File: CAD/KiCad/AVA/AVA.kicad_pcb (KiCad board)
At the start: 2 copper layers, 100 x 75 mm, 47 parts, among them J1 Conn_01x03_Pin, J10 Conn_01x04_Pin, J2 Conn_01x03_Pin, J3 Conn_01x03_Pin, J4 Conn_01x03_Pin, J5 Conn_01x02_Pin, J6 Conn_01x02_Pin, J7 Conn_01x02_Pin, J8 Conn_01x03_Pin, J9 Conn_01x03_Pin

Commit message: Using correct footprint now. Jarvis, more alcohol
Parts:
- added U1: ~, AVA:ESP32-C3-Super-Mini, F.Cu at (204.3, 72.9)
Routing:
- net Net-(U1-D2): track 22.7 -> 114.5 mm
- net Net-(U1-D3): track 30.8 -> 113.2 mm
- net Net-(U1-D1): track 42.5 -> 123.6 mm
- net Net-(U1-D0): track 50.0 -> 127.5 mm
- net Net-(U1-3.3V): track 86.0 -> 138.7 mm
- net Net-(U1-RX): track 0.00 -> 51.6 mm
- net Net-(U1-TX): track 0.00 -> 49.1 mm
- net Net-(J1-Pin_1): track 171.4 -> 214.3 mm
- net (no net): track 41.1 -> 0.00 mm, vias 6 -> 0
- net GND: track 0.00 -> 40.4 mm, vias 0 -> 6
- net Net-(A1-D1/TX): track 52.9 -> 79.5 mm
- net Net-(A1-D0/RX): track 46.7 -> 65.7 mm
- net Net-(U1-D10): track 52.8 -> 37.4 mm
- added copper zone on B.Cu, net GND
- removed copper zone on B.Cu, net (none)

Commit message: Back, front finished. Cropped svg for printing, 500 cigarettes
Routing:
- net GND: vias 6 -> 8
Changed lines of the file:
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@@
 			(dxfimperialunits yes)
 			(dxfusepcbnewfont yes)
-			(psnegative no)
+			(psnegative yes)
 			(psa4output no)
 			(plot_black_and_white yes)
@@
 			(crossoutdnponfab yes)
 			(subtractmaskfromsilk no)
-			(outputformat 2)
+			(outputformat 5)
 			(mirror no)
 			(drillshape 0)
 			(scaleselection 1)
-			(outputdirectory "FAB/DRL/")
+			(outputdirectory "FAB/SVG/")
 		)
 	)
@@
 	)
 	(segment
+		(start 163.83 94.615)
+		(end 163.83 104.565)
+		(width 0.8)
+		(layer "F.Cu")
+		(net "GND")
+	)
+	(segment
 		(start 163.83 70.485)
 		(end 163.83 62.23)
@@
 	(segment
 		(start 163.83 84.455)
-		(end 163.83 104.565)
+		(end 163.83 92.71)
 		(width 0.8)
 		(layer "F.Cu")
@@
 		(net "GND")
 	)
+	(segment
+		(start 163.83 92.71)
+		(end 163.83 94.615)
+		(width 0.8)
+		(layer "F.Cu")
+		(net "GND")
+	)
 	(via
 		(at 163.83 104.565)
@@
 	)
 	(via
+		(at 163.83 92.71)
+		(size 1.6)
+		(drill 0.8)
+		(layers "F.Cu" "B.Cu")
+		(net "GND")
+	)
+	(via
 		(at 163.83 70.485)
 		(size 1.6)
@@
 		(net "GND")
 	)
+	(via
+		(at 163.83 94.615)
+		(size 1.6)
+		(drill 0.8)
+		(layers "F.Cu" "B.Cu")
+		(net "GND")
+	)

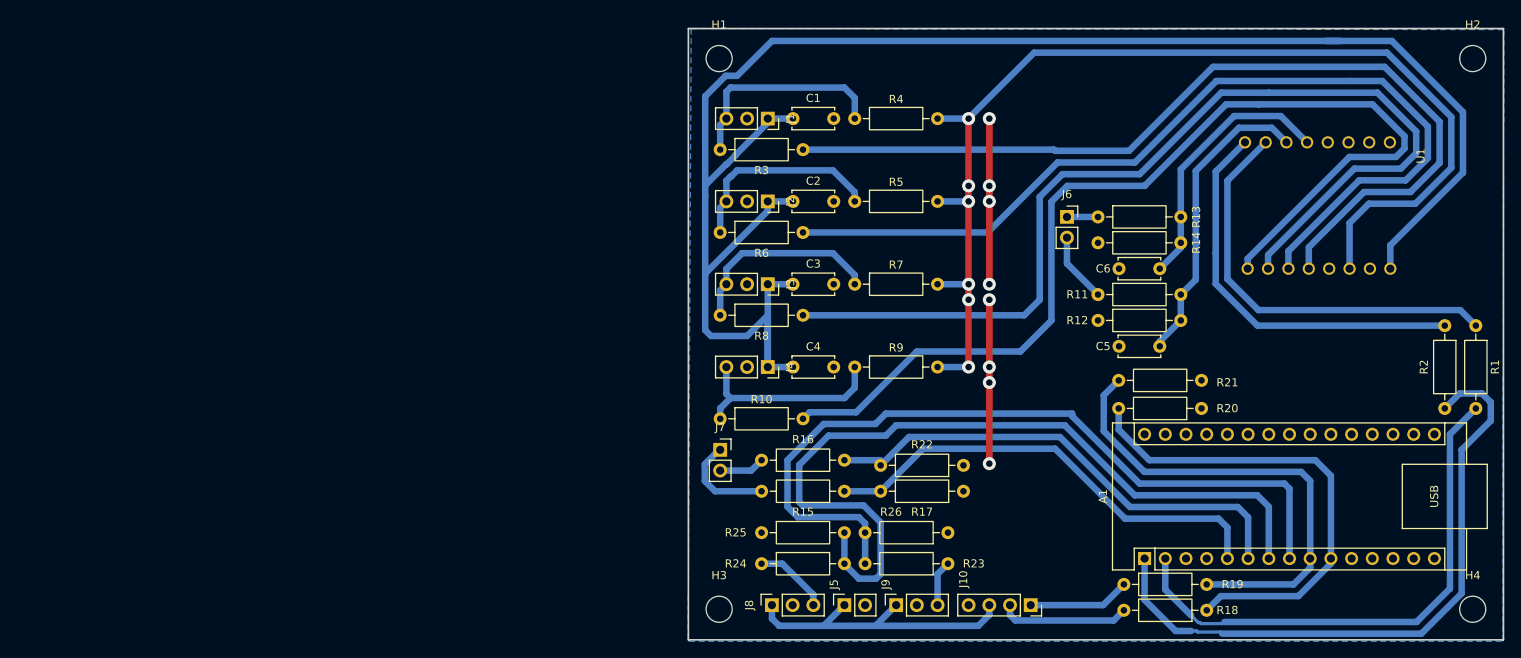
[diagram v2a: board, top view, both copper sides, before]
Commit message: Track width min now 1.6mm. Double sided board, no pre-drawn holes in front, back svg for easy printing
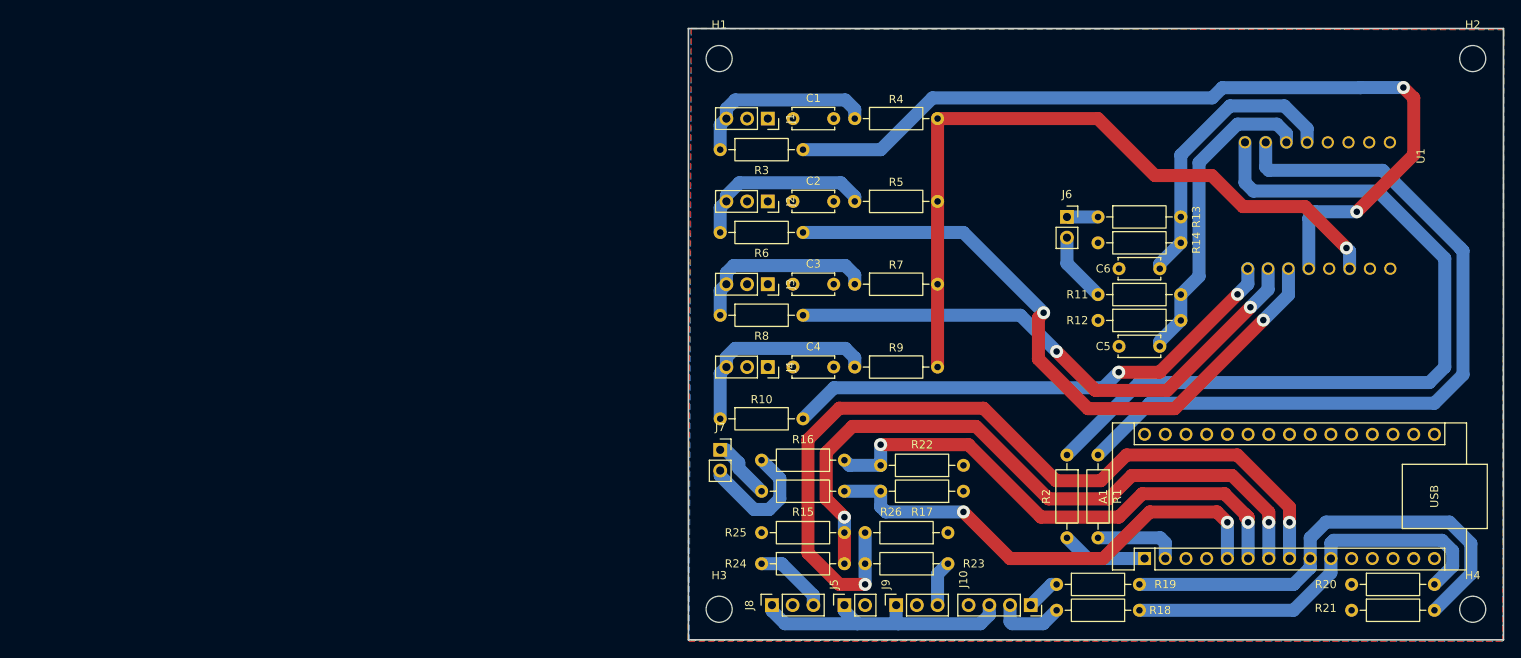
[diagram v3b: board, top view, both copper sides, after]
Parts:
- moved R1 49.0 mm to (177.2, 103.5)
- moved R2 49.0 mm to (173.4, 103.5)
- moved R21 33.7 mm to (208.3, 122.6), turned to 0 degrees
- moved R20 28.4 mm to (208.3, 119.4), turned to 0 degrees
- moved R18 8.25 mm to (182.2, 122.6)
- moved R19 8.25 mm to (172.1, 119.4)
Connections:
- net Net-(J1-Pin_1) renamed VCC
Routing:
- net VCC: track 214.3 -> 0.00 mm
- net Net-(A1-D1/TX): track 79.5 -> 10.6 mm
- net Net-(U1-D0): track 127.5 -> 63.3 mm, vias 0 -> 2
- net Net-(A1-D0/RX): track 65.7 -> 10.4 mm
- net Net-(U1-D1): track 123.6 -> 68.6 mm, vias 0 -> 2
- net Net-(U1-3.3V): track 138.7 -> 89.9 mm, vias 6 -> 1
- net Net-(U1-TX): track 49.1 -> 97.5 mm
- net Net-(U1-RX): track 51.6 -> 95.6 mm
- net GND: track 40.4 -> 0.00 mm, vias 8 -> 0
- net Net-(U1-D2): track 114.5 -> 81.7 mm, vias 0 -> 2
- net Net-(A1-D4): track 101.3 -> 82.6 mm, vias 0 -> 2
- net Net-(J7-Pin_2): track 5.61 -> 15.9 mm
- net Net-(A1-D7): track 59.4 -> 49.7 mm
- net /CH1: track 12.5 -> 4.23 mm
- net /CH2: track 16.0 -> 8.53 mm
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- added copper zone on F.Cu, net VCC

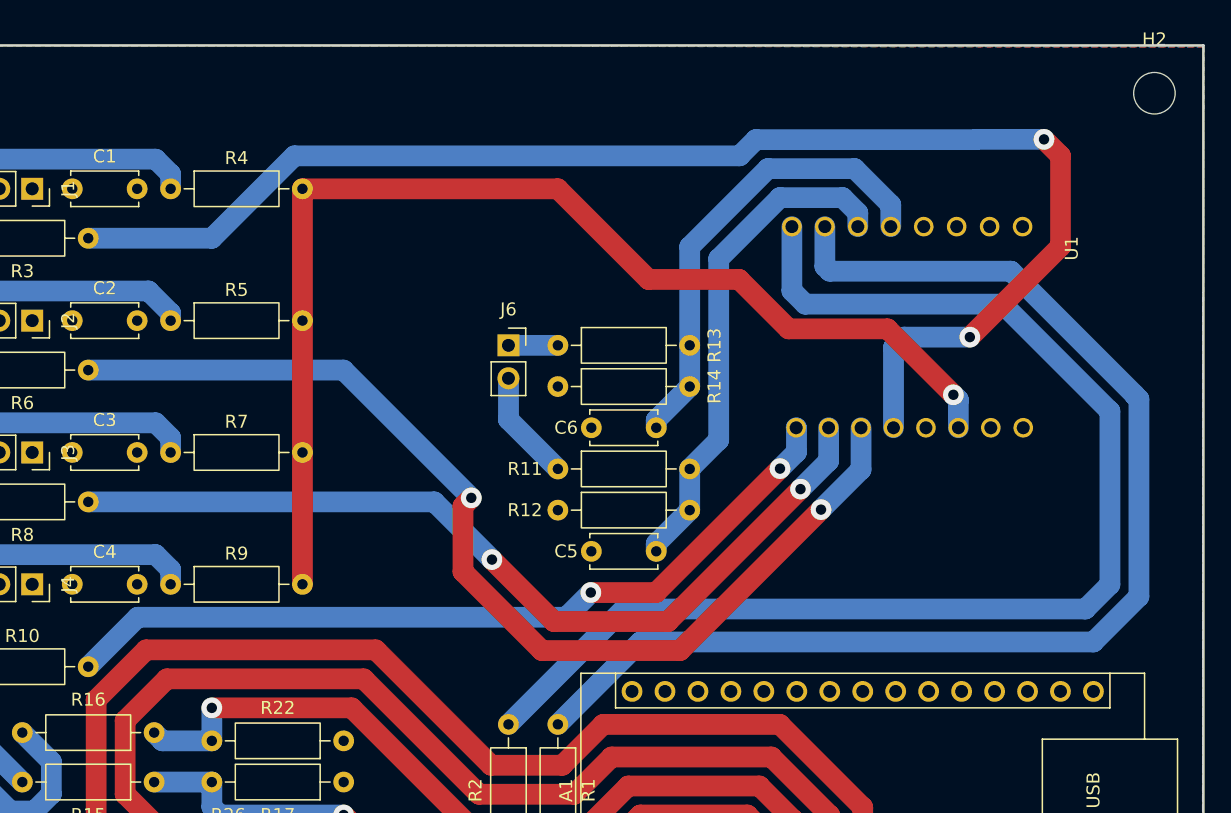
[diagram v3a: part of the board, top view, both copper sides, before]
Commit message: ESP32-C3-SuperMini and Arduino Nano ESP32 layout. Next variant ESP32-C3-SuperMini and ESP32-WROOM-32U
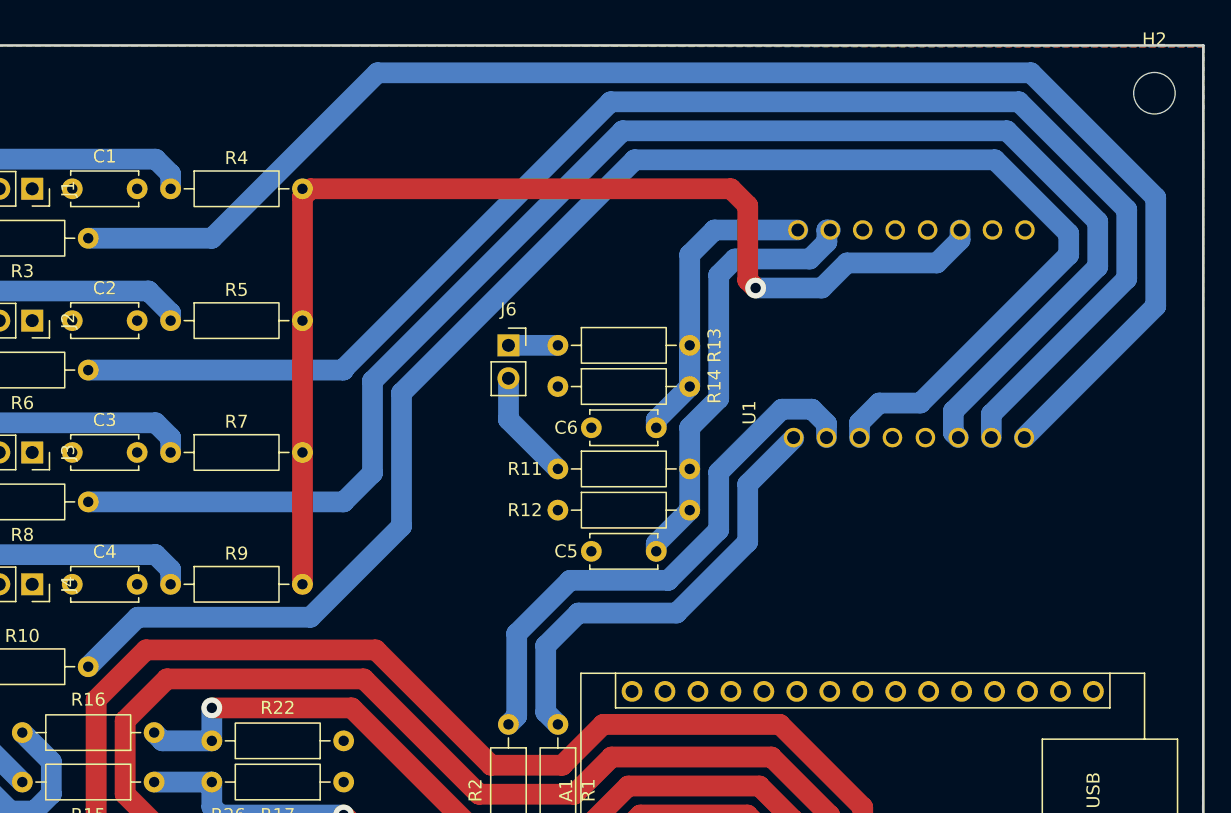
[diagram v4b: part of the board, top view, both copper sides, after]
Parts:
- U1: value ~ -> ESP32-C3-Super-Mini
- moved U1 0.53 mm to (204.4, 73.4), turned to 90 degrees
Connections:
- C5 pad 2: Net-(U1-D10) -> Net-(U1-A1/GPIO1)
- C6 pad 2: Net-(U1-D9) -> Net-(U1-A0/GPIO0)
- R1 pad 1: Net-(U1-RX) -> Net-(U1-TX/GPIO21)
- R10 pad 2: Net-(U1-D0) -> Net-(U1-GPIO10)
- R11 pad 2: Net-(U1-D10) -> Net-(U1-A1/GPIO1)
- R12 pad 2: Net-(U1-D10) -> Net-(U1-A1/GPIO1)
- R13 pad 2: Net-(U1-D9) -> Net-(U1-A0/GPIO0)
- R14 pad 2: Net-(U1-D9) -> Net-(U1-A0/GPIO0)
- R2 pad 1: Net-(U1-TX) -> Net-(U1-RX/GPIO20)
- R3 pad 2: Net-(U1-D3) -> Net-(U1-PISO/GPIO5)
- R6 pad 2: Net-(U1-D2) -> Net-(U1-POSI/GPIO6)
- R8 pad 2: Net-(U1-D1) -> Net-(U1-SS/GPIO7)
- U1 pad 1: unconnected-(U1-D5-Pad1) -> Net-(U1-PISO/GPIO5)
- U1 pad 10: Net-(U1-D1) -> Net-(U1-A1/GPIO1)
- U1 pad 11: Net-(U1-D2) -> unconnected-(U1-A2/GPIO2-Pad11)
- U1 pad 12: Net-(U1-D3) -> unconnected-(U1-A3/GPIO3-Pad12)
- U1 pad 2: unconnected-(U1-D6-Pad2) -> Net-(U1-POSI/GPIO6)
- U1 pad 3: unconnected-(U1-D7-Pad3) -> Net-(U1-SS/GPIO7)
- U1 pad 5: Net-(U1-D9) -> unconnected-(U1-SCLK/GPIO9-Pad5)
- U1 pad 6: Net-(U1-D10) -> Net-(U1-GPIO10)
- U1 pad 7: Net-(U1-RX) -> Net-(U1-RX/GPIO20)
- U1 pad 8: Net-(U1-TX) -> Net-(U1-TX/GPIO21)
- U1 pad 9: Net-(U1-D0) -> Net-(U1-A0/GPIO0)
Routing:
- net Net-(U1-GPIO10): track 0.00 -> 124.4 mm
- net Net-(U1-SS/GPIO7): track 0.00 -> 118.1 mm
- net Net-(U1-PISO/GPIO5): track 0.00 -> 114.2 mm
- net Net-(U1-POSI/GPIO6): track 0.00 -> 114.0 mm
- net Net-(U1-D3): track 107.9 -> 0.00 mm, vias 2 -> 0
- net Net-(U1-TX): track 97.5 -> 0.00 mm
- net Net-(U1-RX): track 95.6 -> 0.00 mm
- net Net-(U1-D2): track 81.7 -> 0.00 mm, vias 2 -> 0
- net Net-(U1-D1): track 68.6 -> 0.00 mm, vias 2 -> 0
- net Net-(U1-D0): track 63.3 -> 0.00 mm, vias 2 -> 0
- net Net-(U1-RX/GPIO20): track 0.00 -> 42.4 mm
- net Net-(U1-D10): track 38.8 -> 0.00 mm
- net Net-(U1-D9): track 35.8 -> 0.00 mm
- net Net-(U1-TX/GPIO21): track 0.00 -> 34.8 mm
- net Net-(U1-A1/GPIO1): track 0.00 -> 33.9 mm
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
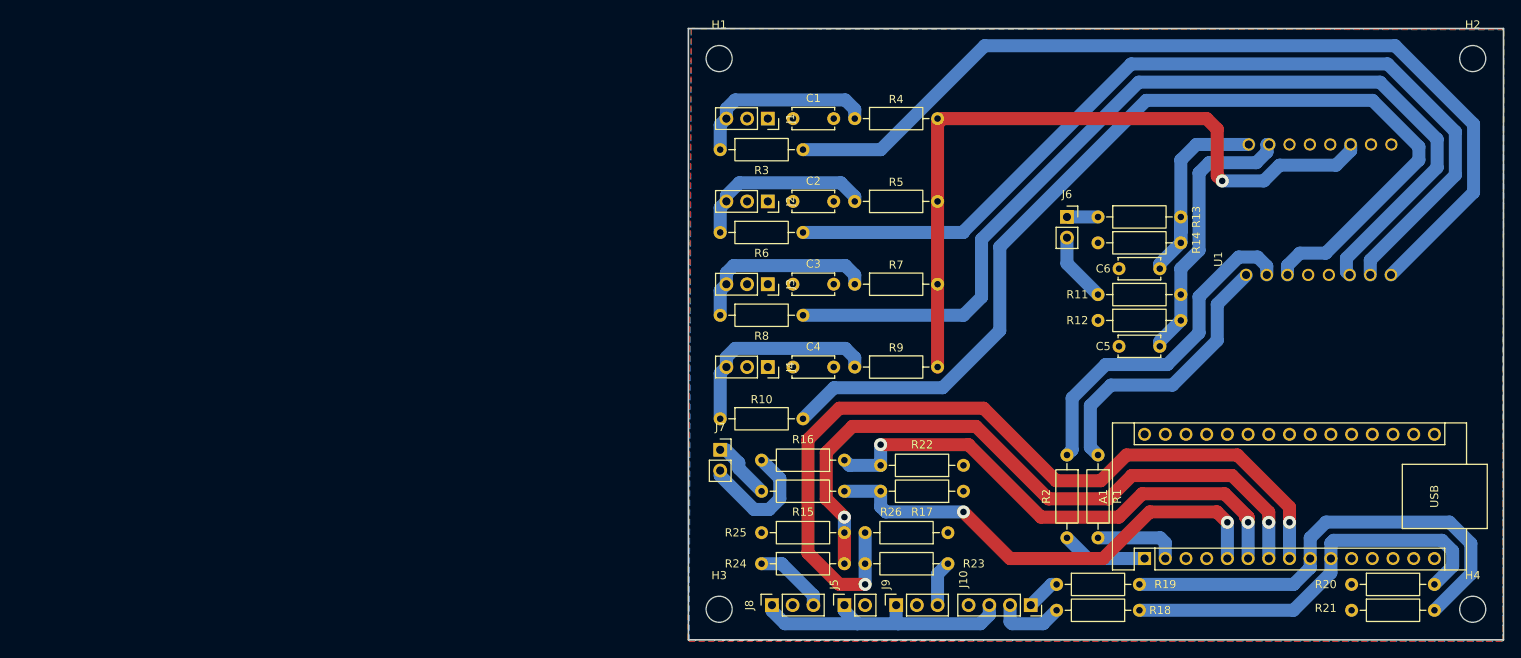
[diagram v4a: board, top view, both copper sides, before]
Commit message: Updated schematic for new ESP32-WROOM-DEVKIT
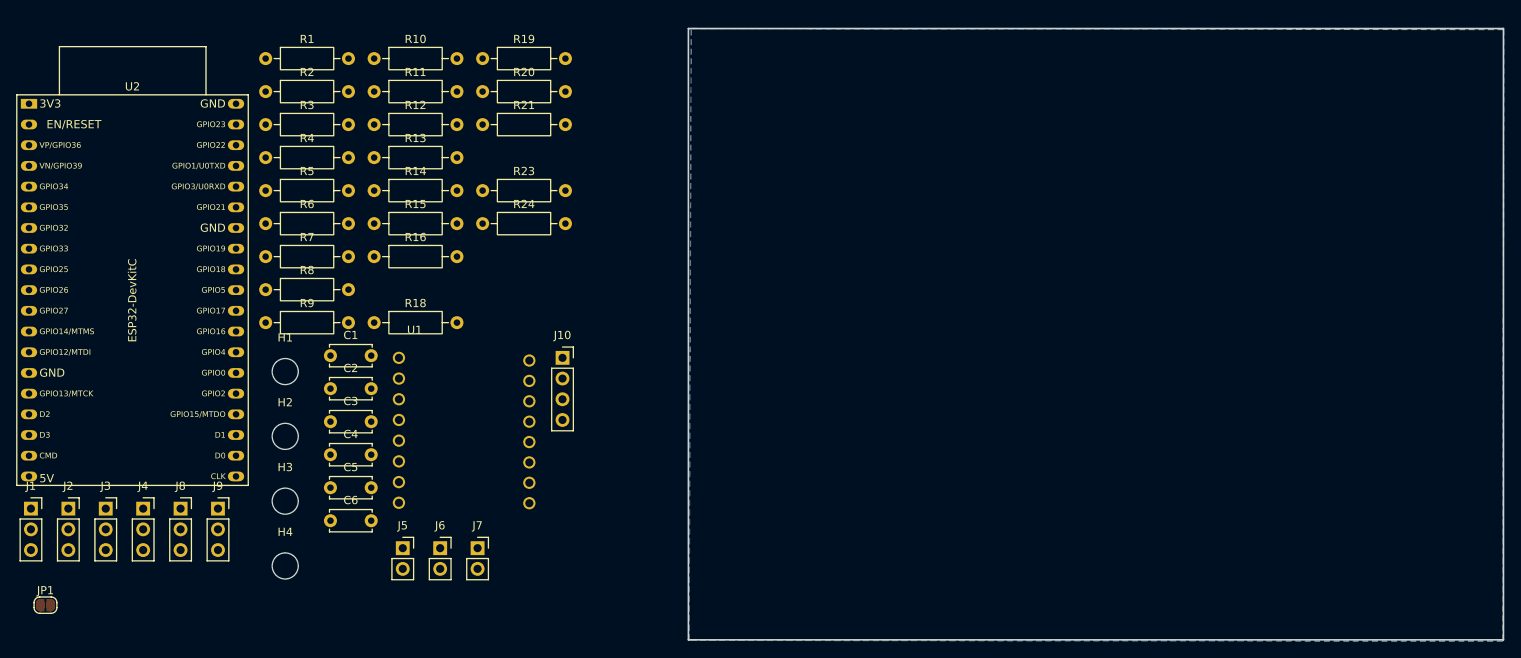
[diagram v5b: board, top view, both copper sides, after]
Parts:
- removed A1: Arduino_Nano_ESP32, Module:Arduino_Nano
- removed R17, R22, R25, R26: 10K, Resistor_THT:R_Axial_DIN0207_L6.3mm_D2.5mm_P10.16mm_Horizontal
- added JP1: SolderJumper_2_Open, Jumper:SolderJumper-2_P1.3mm_Open_RoundedPad1.0x1.5mm, F.Cu at (48.0, 121.9)
- added U2: ESP32-DevKitC, PCM_Espressif:ESP32-DevKitC, F.Cu at (46.0, 60.4)
- moved H2 152.9 mm to (77.4, 101.2)
- moved H4 145.8 mm to (77.4, 117.1)
- moved R20 122.6 mm to (101.7, 58.9)
- moved R21 122.1 mm to (101.7, 63.0)
- moved R1 113.1 mm to (75.0, 54.9), turned to 0 degrees
- moved U1 108.5 mm to (99.4, 100.7), turned to 0 degrees
- moved R2 107.9 mm to (75.0, 58.9), turned to 0 degrees
- moved J1 102.3 mm to (46.2, 110.1), turned to 0 degrees
- moved C6 101.6 mm to (83.0, 111.6)
- moved R18 100.3 mm to (88.4, 87.3), turned to 0 degrees
- moved C5 98.3 mm to (83.0, 107.5)
- moved R19 95.5 mm to (101.7, 54.9)
- moved J2 93.7 mm to (50.8, 110.1), turned to 0 degrees
- moved R11 92.2 mm to (88.4, 58.9)
- moved R12 92.0 mm to (88.4, 63.0)
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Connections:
- R1 pad 1: Net-(U1-TX/GPIO21) -> Net-(U1-RX/GPIO20)
- R2 pad 1: Net-(U1-RX/GPIO20) -> Net-(U1-TX/GPIO21)
- R4 pad 2: Net-(U1-3.3V) -> Net-(JP1-A)
- R5 pad 2: Net-(U1-3.3V) -> Net-(JP1-A)
- R7 pad 2: Net-(U1-3.3V) -> Net-(JP1-A)
- R9 pad 2: Net-(U1-3.3V) -> Net-(JP1-A)
- U1 pad 14: Net-(U1-3.3V) -> Net-(JP1-B)
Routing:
- net Net-(U1-GPIO10): track 124.4 -> 0.00 mm
- net Net-(U1-SS/GPIO7): track 118.1 -> 0.00 mm
- net Net-(U1-PISO/GPIO5): track 114.2 -> 0.00 mm
- net Net-(U1-POSI/GPIO6): track 114.0 -> 0.00 mm
- net Net-(U2-MTDI/GPIO12/ADC2_CH5): track 103.5 -> 0.00 mm, vias 2 -> 0
- net Net-(U1-3.3V): track 89.6 -> 0.00 mm, vias 1 -> 0
- net Net-(U2-MTCK/GPIO13/ADC2_CH4): track 82.6 -> 0.00 mm, vias 2 -> 0
- net Net-(U2-ADC2_CH0/GPIO4): track 63.6 -> 0.00 mm, vias 2 -> 0
- net Net-(U2-ADC2_CH2/GPIO2): track 58.9 -> 0.00 mm, vias 2 -> 0
- net Net-(U2-GPIO5): track 57.1 -> 0.00 mm
- net Net-(U2-GPIO18): track 49.7 -> 0.00 mm
- net Net-(U1-RX/GPIO20): track 42.4 -> 0.00 mm
- net /6.2V: track 35.0 -> 0.00 mm
- net Net-(U1-TX/GPIO21): track 34.8 -> 0.00 mm
- net Net-(U1-A1/GPIO1): track 33.9 -> 0.00 mm
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- removed copper zone on F.Cu, net VCC
